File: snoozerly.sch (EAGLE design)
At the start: 56 parts, among them Q1 MOSFET_PCHANNEL, Q2 MOSFET-NCHANNELFDD8780, Q3 MOSFET-NCHANNELBSS123LT1G, Q4 MOSFET-NCHANNELBSS123LT1G, U1 ATMEGA328P, Y1 32KHz, Y2 8MHz

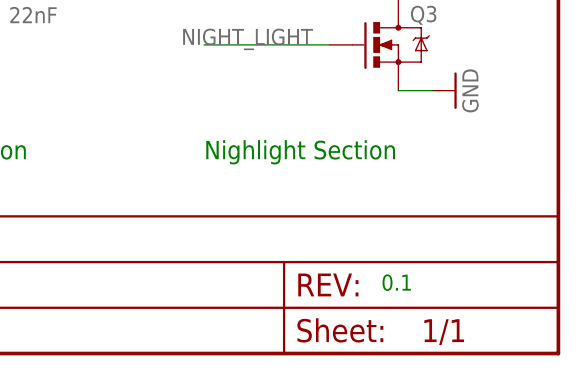
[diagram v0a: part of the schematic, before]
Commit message: added schematic pdf and RTClib for DS1388
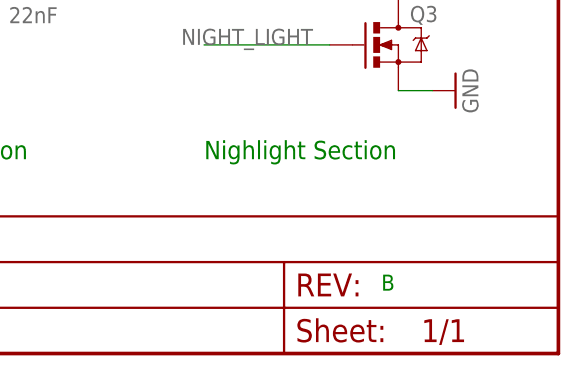
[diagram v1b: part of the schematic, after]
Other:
- note added: "B"
- note removed: "0.1"
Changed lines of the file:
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@@
 <plain>
 <text x="187.325" y="116.205" size="1.778" layer="91">jt lancer</text>
-<text x="244.475" y="116.205" size="1.778" layer="91">0.1</text>
+<text x="244.475" y="116.205" size="1.778" layer="91">B</text>
 <text x="62.23" y="251.46" size="2.032" layer="91">Real Time Clock Section</text>
 <text x="39.37" y="200.66" size="2.032" layer="91">Touch Sensor Section</text>

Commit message: before changing input/output power pads/holes
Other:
- note added: "12V/2A PWM"
- note added: "Display"
- note added: "LCD Backlight"
- note added: "MCU Interface"
- note added: "Microcontroller"
- note added: "Nighlight"
- note added: "Power"
- note added: "Real Time Clock"
- note added: "Touch Sensor"
- note removed: "12V/2A PWM Section"
- note removed: "Display Section"
- note removed: "LCD Backlight Section"
- note removed: "MCU Interface Section"
- note removed: "Microcontroller Section"
- note removed: "Nighlight Section"
- note removed: "Power Section"
- note removed: "Real Time Clock Section"
- note removed: "Touch Sensor Section"
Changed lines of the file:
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@@
 <text x="187.325" y="116.205" size="1.778" layer="91">jt lancer</text>
 <text x="244.475" y="116.205" size="1.778" layer="91">B</text>
-<text x="62.23" y="251.46" size="2.032" layer="91">Real Time Clock Section</text>
-<text x="39.37" y="200.66" size="2.032" layer="91">Touch Sensor Section</text>
-<text x="52.07" y="111.76" size="2.032" layer="91">Microcontroller Section</text>
-<text x="116.84" y="142.24" size="2.032" layer="91">MCU Interface Section</text>
-<text x="179.07" y="130.81" size="2.032" layer="91">12V/2A PWM Section</text>
-<text x="224.79" y="130.81" size="2.032" layer="91">Nighlight Section</text>
-<text x="213.36" y="198.12" size="2.032" layer="91" ratio="10">LCD Backlight Section</text>
-<text x="156.21" y="198.12" size="2.032" layer="91">Display Section</text>
-<text x="162.56" y="262.89" size="2.032" layer="91">Power Section</text>
+<text x="62.23" y="251.46" size="2.032" layer="91">Real Time Clock</text>
+<text x="39.37" y="200.66" size="2.032" layer="91">Touch Sensor</text>
+<text x="52.07" y="111.76" size="2.032" layer="91">Microcontroller</text>
+<text x="116.84" y="142.24" size="2.032" layer="91">MCU Interface</text>
+<text x="179.07" y="130.81" size="2.032" layer="91">12V/2A PWM</text>
+<text x="224.79" y="130.81" size="2.032" layer="91">Nighlight</text>
+<text x="213.36" y="198.12" size="2.032" layer="91" ratio="10">LCD Backlight</text>
+<text x="156.21" y="198.12" size="2.032" layer="91">Display</text>
+<text x="162.56" y="262.89" size="2.032" layer="91">Power</text>
 <text x="212.09" y="284.48" size="1.778" layer="91">3.3V</text>
 </plain>

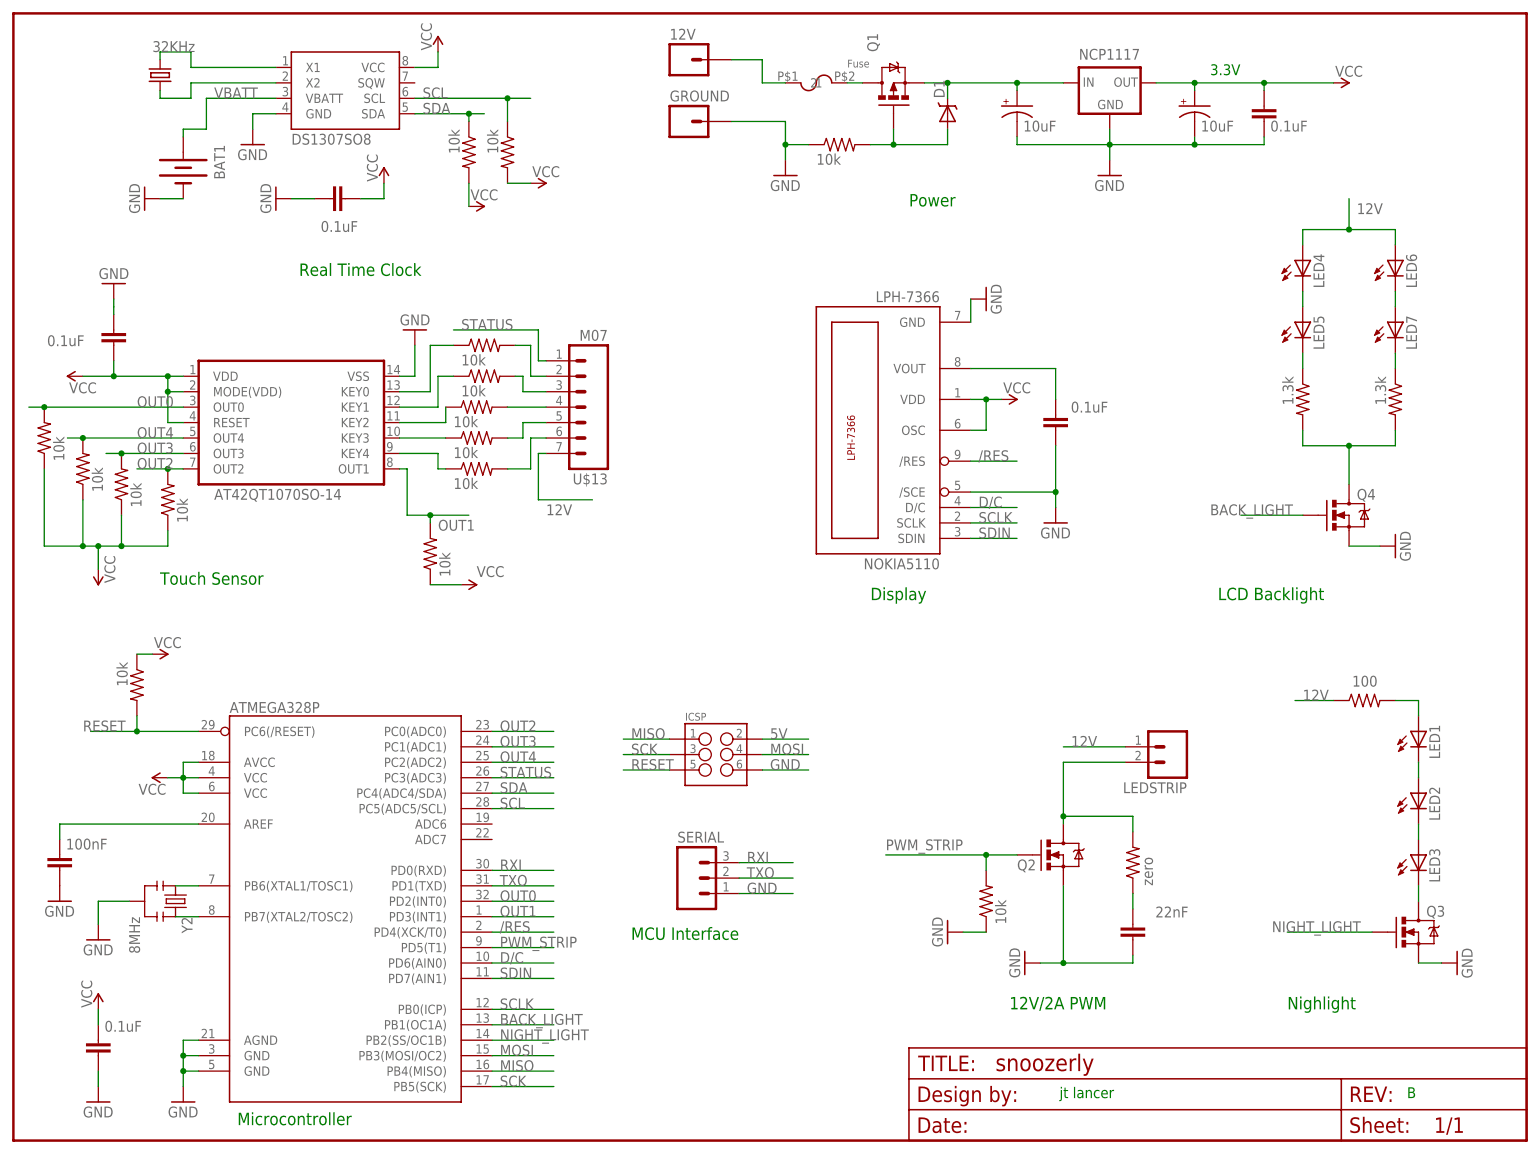
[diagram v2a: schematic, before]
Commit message: added big power holes
rerouted traces around corners. put test/prog headers on 0.1" center
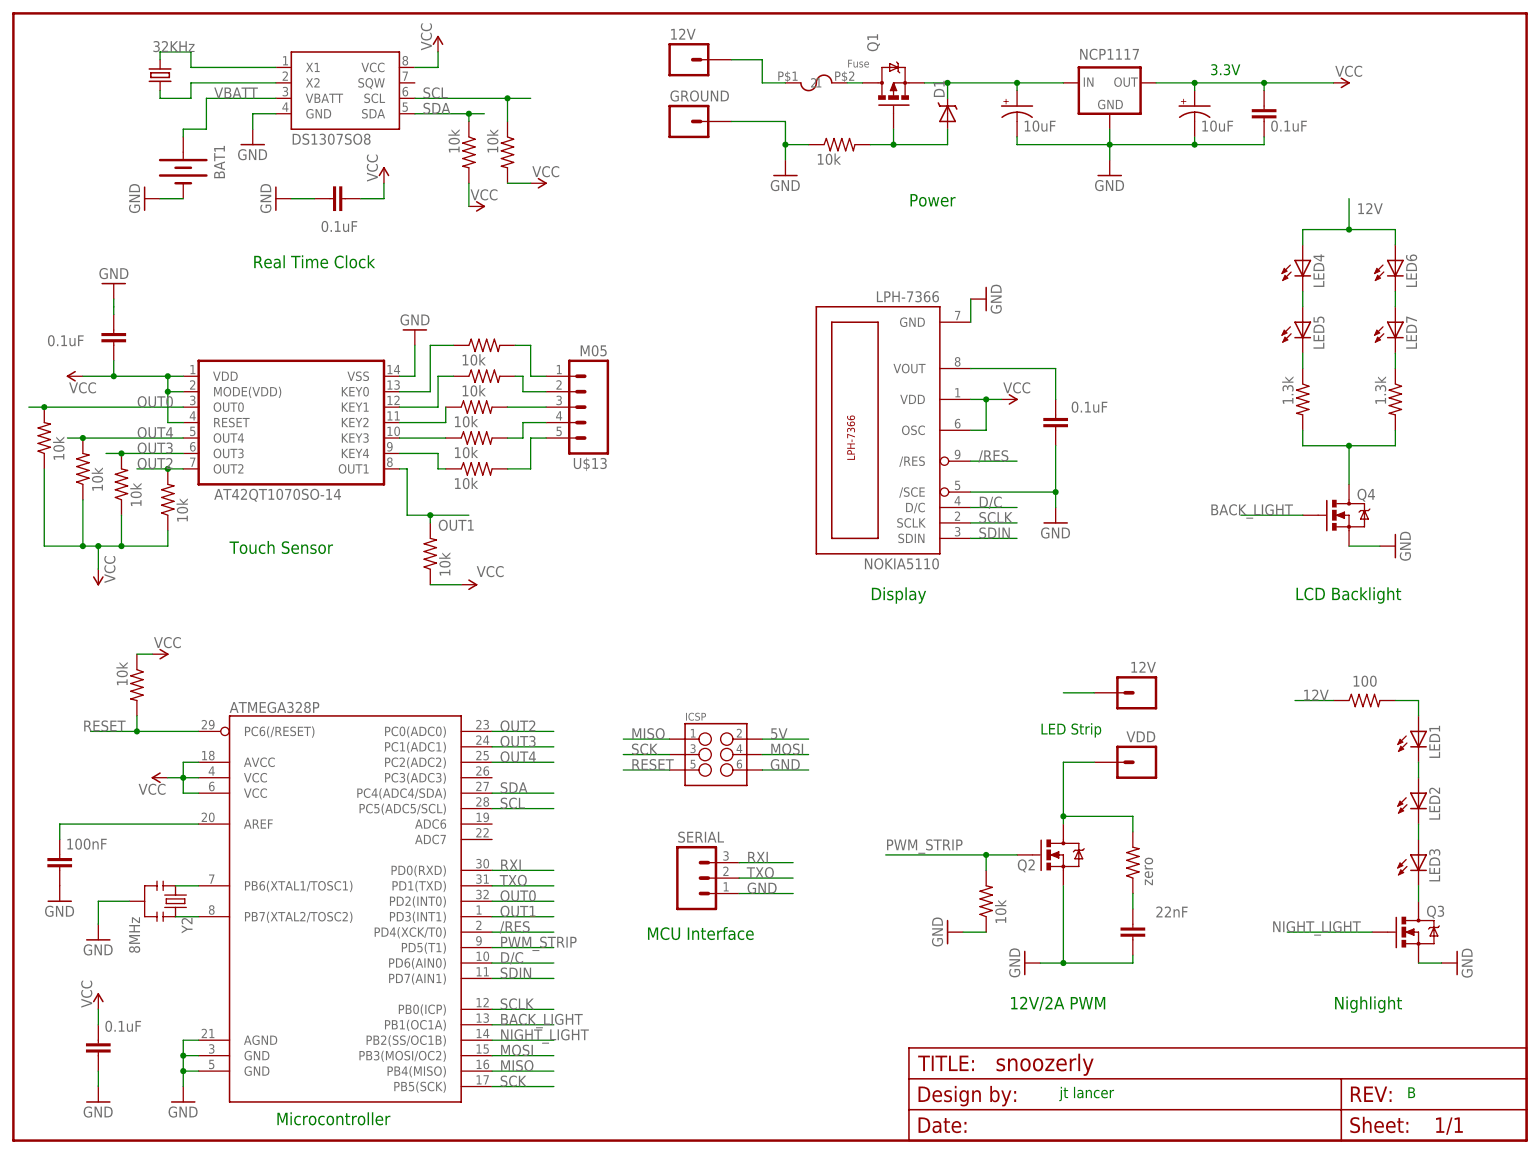
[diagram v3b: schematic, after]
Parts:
- removed LEDSTRIP: M02LOCK_LONGPADS, SparkFun-Connectors:M02LOCK_LONGPADS
- added U$26: VDD, jt_parts:M01
- added U$27: 12V, jt_parts:M01
- 12V, GROUND: value M01PTH_LONGPAD -> M01; device SparkFun-Connectors:M01PTH_LONGPAD -> jt_parts:M01
- U$13: value M07 -> M05; device jt_parts:M07 -> jt_parts:M05
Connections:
- removed net STATUS: U$13.1, U1.PC3(ADC3)
- net 12V: now also U$27.1; no longer LEDSTRIP.1, U$13.7
- net N$14: now also U$26.1; no longer LEDSTRIP.2
- net N$19: now also U$13.3; no longer U$13.4
- net N$21: now also U$13.5; no longer U$13.6
- net N$28: now also U$13.4; no longer U$13.5
- net N$30: now also U$13.2; no longer U$13.3
- net N$31: now also U$13.1; no longer U$13.2
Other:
- note added: "LED Strip"
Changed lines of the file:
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@@
 <setting verticaltext="up"/>
 </settings>
-<grid distance="0.1" unitdist="inch" unit="inch" style="lines" multiple="1" display="no" altdistance="0.01" altunitdist="inch" altunit="inch"/>
+<grid distance="0.05" unitdist="inch" unit="inch" style="lines" multiple="1" display="no" altdistance="0.01" altunitdist="inch" altunit="inch"/>
 <layers>
 <layer number="1" name="Top" color="4" fill="1" visible="no" active="no"/>
@@
 <part name="GND4" library="SparkFun-Aesthetics" deviceset="GND" device=""/>
 <part name="GND6" library="SparkFun-Aesthetics" deviceset="GND" device=""/>
-<part name="LEDSTRIP" library="SparkFun-Connectors" deviceset="M02" device="LOCK_LONGPADS"/>
 <part name="LED1" library="jt_parts" deviceset="LED" device="" value=""/>
 <part name="LED2" library="jt_parts" deviceset="LED" device="" value=""/>
@@
 <part name="ICSP" library="SparkFun-Connectors" deviceset="M03X2" device="POGO_PINS"/>
 <part name="Q4" library="SparkFun-DiscreteSemi" deviceset="MOSFET-NCHANNEL" device="BSS123LT1G"/>
-<part name="12V" library="SparkFun-Connectors" deviceset="M01" device="PTH_LONGPAD"/>
-<part name="GROUND" library="SparkFun-Connectors" deviceset="M01" device="PTH_LONGPAD"/>
-<part name="U$13" library="jt_parts" deviceset="M07" device=""/>
+<part name="12V" library="jt_parts" deviceset="M01" device=""/>
+<part name="GROUND" library="jt_parts" deviceset="M01" device=""/>
 <part name="U$23" library="adafruit" deviceset="R-US_" device="R0603" value="10k"/>
 <part name="SUPPLY6" library="SparkFun-Aesthetics" deviceset="VCC" device="">
@@
 <part name="C9" library="SparkFun-Capacitors" deviceset="CAP" device="0805" value="0.1uF"/>
 <part name="GND7" library="SparkFun-Aesthetics" deviceset="GND" device=""/>
+<part name="U$26" library="jt_parts" deviceset="M01" device="" value="VDD"/>
+<part name="U$27" library="jt_parts" deviceset="M01" device="" value="12V"/>
+<part name="U$13" library="jt_parts" deviceset="M05" device=""/>
 </parts>
 <sheets>
@@
 <text x="187.325" y="116.205" size="1.778" layer="91">jt lancer</text>
 <text x="244.475" y="116.205" size="1.778" layer="91">B</text>
-<text x="62.23" y="251.46" size="2.032" layer="91">Real Time Clock</text>
-<text x="39.37" y="200.66" size="2.032" layer="91">Touch Sensor</text>
-<text x="52.07" y="111.76" size="2.032" layer="91">Microcontroller</text>
-<text x="116.84" y="142.24" size="2.032" layer="91">MCU Interface</text>
+<text x="54.61" y="252.73" size="2.032" layer="91">Real Time Clock</text>
+<text x="50.8" y="205.74" size="2.032" layer="91">Touch Sensor</text>
+<text x="58.42" y="111.76" size="2.032" layer="91">Microcontroller</text>
+<text x="119.38" y="142.24" size="2.032" layer="91">MCU Interface</text>
 <text x="179.07" y="130.81" size="2.032" layer="91">12V/2A PWM</text>
-<text x="224.79" y="130.81" size="2.032" layer="91">Nighlight</text>
-<text x="213.36" y="198.12" size="2.032" layer="91" ratio="10">LCD Backlight</text>
+<text x="232.41" y="130.81" size="2.032" layer="91">Nighlight</text>
+<text x="226.06" y="198.12" size="2.032" layer="91" ratio="10">LCD Backlight</text>
 <text x="156.21" y="198.12" size="2.032" layer="91">Display</text>
 <text x="162.56" y="262.89" size="2.032" layer="91">Power</text>
 <text x="212.09" y="284.48" size="1.778" layer="91">3.3V</text>
+<text x="194.31" y="177.8" size="1.778" layer="91" rot="R180">LED Strip</text>
 </plain>
 <instances>
@@
 <instance part="GND4" gate="1" x="195.58" y="267.97"/>
 <instance part="GND6" gate="1" x="181.61" y="138.43" rot="R270"/>
-<instance part="LEDSTRIP" gate="G$1" x="205.74" y="173.99" smashed="yes" rot="R180">
-<attribute name="NAME" x="208.28" y="168.148" size="1.778" layer="95" rot="R180"/>
-</instance>
 <instance part="LED1" gate="G$1" x="246.38" y="173.99"/>
 <instance part="LED2" gate="G$1" x="246.38" y="163.83"/>
@@
 <attribute name="NAME" x="123.19" y="280.162" size="1.778" layer="95"/>
 </instance>
-<instance part="U$13" gate="G$1" x="107.95" y="229.87" rot="R180"/>
 <instance part="U$23" gate="G$1" x="83.82" y="205.74" smashed="yes" rot="R90">
 <attribute name="VALUE" x="87.122" y="201.93" size="1.778" layer="96" rot="R90"/>
@@
 <attribute name="VALUE" x="34.29" y="252.73" size="1.778" layer="96" rot="R180"/>
 </instance>
+<instance part="U$26" gate="G$1" x="200.66" y="171.45" smashed="yes" rot="R180">
+<attribute name="VALUE" x="203.2" y="176.53" size="1.778" layer="96" rot="R180"/>
+</instance>
+<instance part="U$27" gate="G$1" x="200.66" y="182.88" smashed="yes" rot="R180">
+<attribute name="VALUE" x="203.2" y="187.96" size="1.778" layer="96" rot="R180"/>
+</instance>
+<instance part="U$13" gate="G$1" x="110.49" y="229.87" rot="R180"/>
 </instances>
 <busses>
@@
 <net name="12V" class="0">
 <segment>
-<pinref part="LEDSTRIP" gate="G$1" pin="1"/>
-<wire x1="198.12" y1="173.99" x2="187.96" y2="173.99" width="0.1524" layer="91"/>
-<label x="189.23" y="173.99" size="1.778" layer="95"/>
+<wire x1="193.04" y1="182.88" x2="187.96" y2="182.88" width="0.1524" layer="91"/>
+<pinref part="U$27" gate="G$1" pin="1"/>
 </segment>
 <segment>
@@
 <label x="227.33" y="181.61" size="1.778" layer="95"/>
 </segment>
-<segment>
-<pinref part="U$13" gate="G$1" pin="7"/>
-<wire x1="102.87" y1="222.25" x2="101.6" y2="222.25" width="0.1524" layer="91"/>
-<wire x1="101.6" y1="222.25" x2="101.6" y2="214.63" width="0.1524" layer="91"/>
-<wire x1="101.6" y1="214.63" x2="110.49" y2="214.63" width="0.1524" layer="91"/>
-<label x="102.87" y="212.09" size="1.778" layer="95"/>
-</segment>
 </net>
 <net name="N$14" class="1">
 <segment>
-<pinref part="LEDSTRIP" gate="G$1" pin="2"/>
-<wire x1="198.12" y1="171.45" x2="187.96" y2="171.45" width="0.1524" layer="91"/>
+<wire x1="193.04" y1="171.45" x2="187.96" y2="171.45" width="0.1524" layer="91"/>
 <wire x1="199.39" y1="162.56" x2="187.96" y2="162.56" width="0.1524" layer="91"/>
 <pinref part="Q2" gate="G$1" pin="D"/>
@@
 <pinref part="U$25" gate="G$1" pin="2"/>
 <wire x1="199.39" y1="160.02" x2="199.39" y2="162.56" width="0.1524" layer="91"/>
+<pinref part="U$26" gate="G$1" pin="1"/>
 </segment>
 </net>
@@
 <wire x1="96.52" y1="219.71" x2="100.33" y2="219.71" width="0.1524" layer="91"/>
 <wire x1="100.33" y1="219.71" x2="100.33" y2="224.79" width="0.1524" layer="91"/>
-<pinref part="U$13" gate="G$1" pin="6"/>
-<wire x1="102.87" y1="224.79" x2="100.33" y2="224.79" width="0.1524" layer="91"/>
+<pinref part="U$13" gate="G$1" pin="5"/>
+<wire x1="100.33" y1="224.79" x2="102.87" y2="224.79" width="0.1524" layer="91"/>
 </segment>
 </net>
@@
 <wire x1="96.52" y1="224.79" x2="99.06" y2="224.79" width="0.1524" layer="91"/>
 <wire x1="99.06" y1="224.79" x2="99.06" y2="227.33" width="0.1524" layer="91"/>
-<pinref part="U$13" gate="G$1" pin="5"/>
+<pinref part="U$13" gate="G$1" pin="4"/>
 <wire x1="102.87" y1="227.33" x2="99.06" y2="227.33" width="0.1524" layer="91"/>
 </segment>
@@
 <wire x1="97.79" y1="234.95" x2="99.06" y2="234.95" width="0.1524" layer="91"/>
 <wire x1="99.06" y1="234.95" x2="99.06" y2="232.41" width="0.1524" layer="91"/>
-<pinref part="U$13" gate="G$1" pin="3"/>
-<wire x1="102.87" y1="232.41" x2="99.06" y2="232.41" width="0.1524" layer="91"/>
+<pinref part="U$13" gate="G$1" pin="2"/>
+<wire x1="99.06" y1="232.41" x2="102.87" y2="232.41" width="0.1524" layer="91"/>
 </segment>
 </net>
@@
 <wire x1="97.79" y1="240.03" x2="100.33" y2="240.03" width="0.1524" layer="91"/>
 <wire x1="100.33" y1="240.03" x2="100.33" y2="234.95" width="0.1524" layer="91"/>
-<pinref part="U$13" gate="G$1" pin="2"/>
-<wire x1="102.87" y1="234.95" x2="100.33" y2="234.95" width="0.1524" layer="91"/>
+<pinref part="U$13" gate="G$1" pin="1"/>
+<wire x1="100.33" y1="234.95" x2="102.87" y2="234.95" width="0.1524" layer="91"/>
 </segment>
 </net>
@@
 </segment>
 </net>
-<net name="N$19" class="0">
-<segment>
-<pinref part="U$13" gate="G$1" pin="4"/>
-<pinref part="U$9" gate="G$1" pin="2"/>
-<wire x1="102.87" y1="229.87" x2="96.52" y2="229.87" width="0.1524" layer="91"/>
-</segment>
-</net>
-<net name="STATUS" class="0">
-<segment>
-<pinref part="U1" gate="G$1" pin="PC3(ADC3)"/>
-<wire x1="93.98" y1="168.91" x2="104.14" y2="168.91" width="0.1524" layer="91"/>
-<label x="95.25" y="168.91" size="1.778" layer="95"/>
-</segment>
-<segment>
-<wire x1="101.6" y1="242.57" x2="87.63" y2="242.57" width="0.1524" layer="91"/>
-<label x="88.9" y="242.57" size="1.778" layer="95"/>
-<pinref part="U$13" gate="G$1" pin="1"/>
-<wire x1="102.87" y1="237.49" x2="101.6" y2="237.49" width="0.1524" layer="91"/>
-<wire x1="101.6" y1="237.49" x2="101.6" y2="242.57" width="0.1524" layer="91"/>
-</segment>
-</net>
 <net name="PWM_STRIP" class="0">
 <segment>
@@
 </segment>
 </net>
+<net name="N$19" class="0">
+<segment>
+<pinref part="U$9" gate="G$1" pin="2"/>
+<pinref part="U$13" gate="G$1" pin="3"/>
+<wire x1="96.52" y1="229.87" x2="102.87" y2="229.87" width="0.1524" layer="91"/>
+</segment>
+</net>
